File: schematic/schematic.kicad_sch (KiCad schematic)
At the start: 19 parts, among them J1 Analog, J2 Digital, U1 74HC595

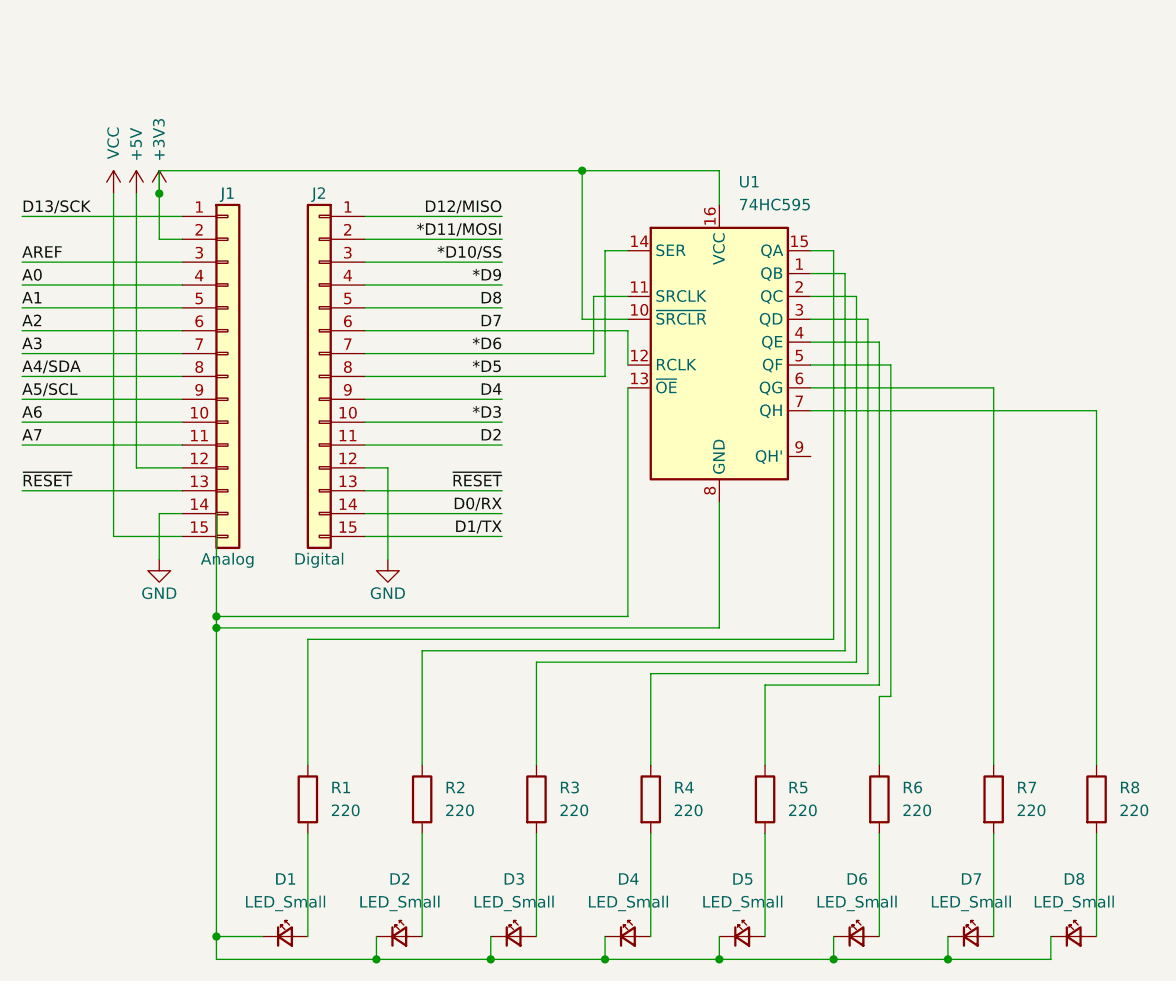
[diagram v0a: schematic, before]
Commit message: Update schematic and swap pins for simplification
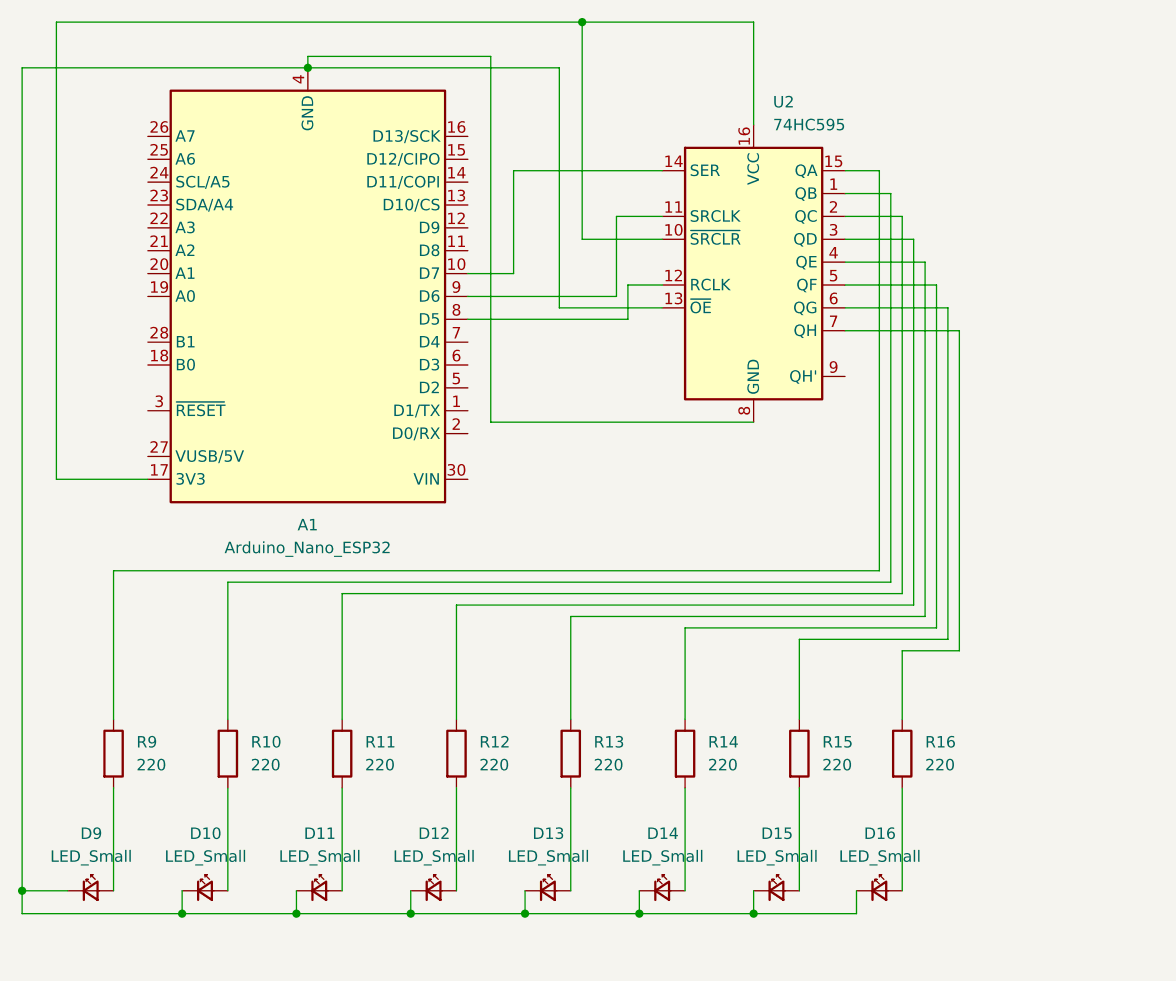
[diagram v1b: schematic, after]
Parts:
- removed D1, D2, D3, D4, D5, D6, D7, D8: LED_Small, LED_THT:LED_D5.0mm, symbol Device:LED_Small
- removed J1: Analog, Connector_PinHeader_2.54mm:PinHeader_1x15_P2.54mm_Vertical, symbol Connector_Generic:Conn_01x15
- removed J2: Digital, Connector_PinHeader_2.54mm:PinHeader_1x15_P2.54mm_Vertical, symbol Connector_Generic:Conn_01x15
- removed R1, R2, R3, R4, R5, R6, R7, R8: 220, Resistor_SMD:R_0508_1220Metric, symbol Device:R
- removed U1: 74HC595, Package_DIP:DIP-16_W7.62mm, symbol 74xx:74HC595
- added A1: Arduino_Nano_ESP32, Module:Arduino_Nano, symbol MCU_Module:Arduino_Nano_ESP32
- added D10, D11, D12, D13, D14, D15, D16, D9: LED_Small, LED_THT:LED_D5.0mm, symbol Device:LED_Small
- added R10, R11, R12, R13, R14, R15, R16, R9: 220, Resistor_SMD:R_0508_1220Metric, symbol Device:R
- added U2: 74HC595, Package_DIP:DIP-16_W7.62mm, symbol 74xx:74HC595
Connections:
- new net: R9.1, U2.15 (QA)
- new net: D9.2 (A), R9.2
- new net: A1.10 (D7), U2.14 (SER)
- new net: A1.17 (3V3), U2.10 (~{SRCLR}), U2.16 (VCC)
- new net: A1.29 (GND), A1.4 (GND), D10.1 (K), D11.1 (K), D12.1 (K), D13.1 (K), D14.1 (K), D15.1 (K), D16.1 (K), D9.1 (K), U2.13 (~{OE}), U2.8 (GND)
- new net: A1.8 (D5), U2.12 (RCLK)
- new net: A1.9 (D6), U2.11 (SRCLK)
- new net: R14.1, U2.5 (QF)
- new net: D14.2 (A), R14.2
- new net: D15.2 (A), R15.2
- new net: R13.1, U2.4 (QE)
- new net: D13.2 (A), R13.2
- new net: D11.2 (A), R11.2
- new net: D10.2 (A), R10.2
- new net: R12.1, U2.3 (QD)
- new net: D12.2 (A), R12.2
- new net: R16.1, U2.7 (QH)
- new net: D16.2 (A), R16.2
- new net: R15.1, U2.6 (QG)
- new net: R10.1, U2.1 (QB)
- new net: R11.1, U2.2 (QC)

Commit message: Update schematic to use correct, non-surface mount resistors
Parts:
- R10, R11, R12, R13, R14, R15, R16, R9: footprint Resistor_SMD:R_0508_1220Metric -> Resistor_THT:R_Axial_DIN0207_L6.3mm_D2.5mm_P7.62mm_Horizontal
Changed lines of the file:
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@@
 			)
 		)
-		(property "Footprint" "Resistor_SMD:R_0508_1220Metric"
+		(property "Footprint" "Resistor_THT:R_Axial_DIN0207_L6.3mm_D2.5mm_P7.62mm_Horizontal"
 			(at 97.282 124.46 90)
 			(hide yes)
@@
 			)
 		)
-		(property "Footprint" "Resistor_SMD:R_0508_1220Metric"
+		(property "Footprint" "Resistor_THT:R_Axial_DIN0207_L6.3mm_D2.5mm_P7.62mm_Horizontal"
 			(at 160.782 124.46 90)
 			(hide yes)
@@
 			)
 		)
-		(property "Footprint" "Resistor_SMD:R_0508_1220Metric"
+		(property "Footprint" "Resistor_THT:R_Axial_DIN0207_L6.3mm_D2.5mm_P7.62mm_Horizontal"
 			(at 148.082 124.46 90)
 			(hide yes)
@@
 			)
 		)
-		(property "Footprint" "Resistor_SMD:R_0508_1220Metric"
+		(property "Footprint" "Resistor_THT:R_Axial_DIN0207_L6.3mm_D2.5mm_P7.62mm_Horizontal"
 			(at 135.382 124.46 90)
 			(hide yes)
@@
 			)
 		)
-		(property "Footprint" "Resistor_SMD:R_0508_1220Metric"
+		(property "Footprint" "Resistor_THT:R_Axial_DIN0207_L6.3mm_D2.5mm_P7.62mm_Horizontal"
 			(at 184.912 124.46 90)
 			(hide yes)
@@
 			)
 		)
-		(property "Footprint" "Resistor_SMD:R_0508_1220Metric"
+		(property "Footprint" "Resistor_THT:R_Axial_DIN0207_L6.3mm_D2.5mm_P7.62mm_Horizontal"
 			(at 173.482 124.46 90)
 			(hide yes)
@@
 			)
 		)
-		(property "Footprint" "Resistor_SMD:R_0508_1220Metric"
+		(property "Footprint" "Resistor_THT:R_Axial_DIN0207_L6.3mm_D2.5mm_P7.62mm_Horizontal"
 			(at 109.982 124.46 90)
 			(hide yes)
@@
 			)
 		)
-		(property "Footprint" "Resistor_SMD:R_0508_1220Metric"
+		(property "Footprint" "Resistor_THT:R_Axial_DIN0207_L6.3mm_D2.5mm_P7.62mm_Horizontal"
 			(at 122.682 124.46 90)
 			(hide yes)
